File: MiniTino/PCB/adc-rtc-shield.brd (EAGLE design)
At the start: 68.6 x 53.3 mm, 57 parts, among them IC1 TLC2543, IC2 RV_3049_C2

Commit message: Aktualisiert.
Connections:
- net +5V: now also U$1.21
- net A6: now also U$1.A6
- net A7: now also U$1.A7
- net AD0: now also U$1.17
- net AD1: now also U$1.18
- net AD2: now also U$1.19
- net AD3: now also U$1.20
- net AD4/SDA: now also U$1.A4
- net AD5/SCL: now also U$1.A5
- net GND: now also U$1.23
- net IO0: now also U$1.2
- net IO1: now also U$1.1
- net IO2: now also U$1.5
- net IO3: now also U$1.6
- net IO4: now also U$1.7
- net IO5: now also U$1.8
- net IO6: now also U$1.9
- net IO7: now also U$1.10
- net IO8: now also U$1.11
- net IO9: now also U$1.12
- net MISO: now also U$1.15
- net MOSI: now also U$1.14
- net RESET: now also U$1.3
- net SCK: now also U$1.16
- net SS: now also U$1.13
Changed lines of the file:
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@@
 <layer number="49" name="ReferenceLC" color="13" fill="1" visible="no" active="yes"/>
 <layer number="50" name="ReferenceLS" color="12" fill="1" visible="no" active="yes"/>
-<layer number="51" name="tDocu" color="7" fill="1" visible="no" active="yes"/>
+<layer number="51" name="tDocu" color="7" fill="1" visible="yes" active="yes"/>
 <layer number="52" name="bDocu" color="7" fill="1" visible="no" active="yes"/>
 <layer number="91" name="Nets" color="2" fill="1" visible="no" active="no"/>
@@
 <contactref element="JP7" pad="1"/>
 <contactref element="POWER" pad="2"/>
+<contactref element="U$1" pad="21"/>
 <wire x1="40.64" y1="34.29" x2="42.18" y2="36.83" width="0" layer="19" extent="16-16"/>
 <wire x1="34.645" y1="39.91" x2="42.18" y2="36.83" width="0" layer="19" extent="16-16"/>
@@
 <wire x1="38.1" y1="2.54" x2="30.48" y2="2.54" width="0" layer="19" extent="1-1"/>
 <wire x1="44.45" y1="6.35" x2="38.1" y2="2.54" width="0" layer="19" extent="1-1"/>
+<wire x1="-8.89" y1="21.59" x2="7.62" y2="6.35" width="0" layer="19" extent="1-1"/>
 </signal>
 <signal name="GND" class="2">
@@
 <contactref element="JP2" pad="1"/>
 <contactref element="JP3" pad="1"/>
+<contactref element="U$1" pad="23"/>
 <wire x1="44.45" y1="31.75" x2="44.18" y2="36.83" width="0" layer="19" extent="16-16"/>
 <wire x1="37.745" y1="43.91" x2="44.18" y2="36.83" width="0" layer="19" extent="16-16"/>
@@
 <wire x1="44.45" y1="14.875" x2="33.02" y2="11.43" width="0" layer="19" extent="16-16"/>
 <wire x1="4.445" y1="13.97" x2="19.05" y2="13.97" width="0" layer="19" extent="1-1"/>
+<wire x1="-8.89" y1="26.67" x2="4.445" y2="13.97" width="0" layer="19" extent="1-1"/>
 </signal>
 <signal name="AREF" class="4">
@@
 <contactref element="IC2" pad="4"/>
 <contactref element="IC1" pad="18"/>
+<contactref element="U$1" pad="16"/>
 <wire x1="34.645" y1="42.91" x2="28.956" y2="50.8" width="0" layer="19" extent="16-16"/>
 <wire x1="40.64" y1="29.21" x2="34.645" y2="42.91" width="0" layer="19" extent="16-16"/>
+<wire x1="-8.89" y1="8.89" x2="40.64" y2="29.21" width="0" layer="19" extent="1-1"/>
 </signal>
 <signal name="+3V3">
@@
 <contactref element="IC2" pad="5"/>
 <contactref element="IC1" pad="16"/>
+<contactref element="U$1" pad="15"/>
 <wire x1="34.645" y1="43.91" x2="31.496" y2="50.8" width="0" layer="19" extent="16-16"/>
 <wire x1="40.64" y1="24.13" x2="34.645" y2="43.91" width="0" layer="19" extent="16-16"/>
+<wire x1="-8.89" y1="6.35" x2="40.64" y2="24.13" width="0" layer="19" extent="1-1"/>
 </signal>
 <signal name="MOSI">
@@
 <contactref element="IC2" pad="9"/>
 <contactref element="IC1" pad="17"/>
+<contactref element="U$1" pad="14"/>
 <wire x1="37.745" y1="40.91" x2="34.036" y2="50.8" width="0" layer="19" extent="16-16"/>
 <wire x1="40.64" y1="26.67" x2="37.745" y2="40.91" width="0" layer="19" extent="16-16"/>
+<wire x1="-8.89" y1="3.81" x2="40.64" y2="26.67" width="0" layer="19" extent="1-1"/>
 </signal>
 <signal name="SS">
 <contactref element="IOH" pad="3"/>
+<contactref element="U$1" pad="13"/>
+<wire x1="-8.89" y1="1.27" x2="36.576" y2="50.8" width="0" layer="19" extent="1-1"/>
 </signal>
 <signal name="AD0">
 <contactref element="AD" pad="1"/>
+<contactref element="U$1" pad="17"/>
+<wire x1="-8.89" y1="11.43" x2="50.8" y2="2.54" width="0" layer="19" extent="1-1"/>
 </signal>
 <signal name="AD1">
 <contactref element="AD" pad="2"/>
+<contactref element="U$1" pad="18"/>
+<wire x1="-8.89" y1="13.97" x2="53.34" y2="2.54" width="0" layer="19" extent="1-1"/>
 </signal>
 <signal name="AD2">
 <contactref element="AD" pad="3"/>
+<contactref element="U$1" pad="19"/>
+<wire x1="-8.89" y1="16.51" x2="55.88" y2="2.54" width="0" layer="19" extent="1-1"/>
 </signal>
 <signal name="AD3">
 <contactref element="AD" pad="4"/>
+<contactref element="U$1" pad="20"/>
+<wire x1="-8.89" y1="19.05" x2="58.42" y2="2.54" width="0" layer="19" extent="1-1"/>
 </signal>
 <signal name="AD4/SDA">
 <contactref element="IOH" pad="9"/>
 <contactref element="IC2" pad="3"/>
+<contactref element="U$1" pad="A4"/>
 <wire x1="21.336" y1="50.8" x2="34.645" y2="41.91" width="0" layer="19" extent="16-16"/>
+<wire x1="-11.7475" y1="17.93875" x2="21.336" y2="50.8" width="0" layer="19" extent="1-1"/>
 </signal>
 <signal name="AD5/SCL">
 <contactref element="IOH" pad="10"/>
 <contactref element="IC1" pad="15"/>
+<contactref element="U$1" pad="A5"/>
 <wire x1="40.64" y1="21.59" x2="18.796" y2="50.8" width="0" layer="19" extent="1-1"/>
+<wire x1="-11.7475" y1="20.47875" x2="18.796" y2="50.8" width="0" layer="19" extent="1-1"/>
 </signal>
 <signal name="IO2">
 <contactref element="IOL" pad="3"/>
+<contactref element="U$1" pad="5"/>
+<wire x1="-24.13" y1="19.05" x2="58.42" y2="50.8" width="0" layer="19" extent="1-1"/>
 </signal>
 <signal name="IO1">
 <contactref element="IOL" pad="2"/>
+<contactref element="U$1" pad="1"/>
+<wire x1="-24.13" y1="29.21" x2="60.96" y2="50.8" width="0" layer="19" extent="1-1"/>
 </signal>
 <signal name="IO0">
 <contactref element="IOL" pad="1"/>
+<contactref element="U$1" pad="2"/>
+<wire x1="-24.13" y1="26.67" x2="63.5" y2="50.8" width="0" layer="19" extent="1-1"/>
 </signal>
 <signal name="IO3">
 <contactref element="IOL" pad="4"/>
+<contactref element="U$1" pad="6"/>
+<wire x1="-24.13" y1="16.51" x2="55.88" y2="50.8" width="0" layer="19" extent="1-1"/>
 </signal>
 <signal name="IO4">
 <contactref element="IOL" pad="5"/>
+<contactref element="U$1" pad="7"/>
+<wire x1="-24.13" y1="13.97" x2="53.34" y2="50.8" width="0" layer="19" extent="1-1"/>
 </signal>
 <signal name="IO5">
 <contactref element="IOL" pad="6"/>
+<contactref element="U$1" pad="8"/>
+<wire x1="-24.13" y1="11.43" x2="50.8" y2="50.8" width="0" layer="19" extent="1-1"/>
 </signal>
 <signal name="IO6">
 <contactref element="IOL" pad="7"/>
+<contactref element="U$1" pad="9"/>
+<wire x1="-24.13" y1="8.89" x2="48.26" y2="50.8" width="0" layer="19" extent="1-1"/>
 </signal>
 <signal name="IO7">
 <contactref element="IOL" pad="8"/>
+<contactref element="U$1" pad="10"/>
+<wire x1="-24.13" y1="6.35" x2="45.72" y2="50.8" width="0" layer="19" extent="1-1"/>
 </signal>
 <signal name="IO8">
 <contactref element="IOH" pad="1"/>
+<contactref element="U$1" pad="11"/>
+<wire x1="-24.13" y1="3.81" x2="41.656" y2="50.8" width="0" layer="19" extent="1-1"/>
 </signal>
 <signal name="IO9">
 <contactref element="IOH" pad="2"/>
+<contactref element="U$1" pad="12"/>
+<wire x1="-24.13" y1="1.27" x2="39.116" y2="50.8" width="0" layer="19" extent="1-1"/>
 </signal>
 <signal name="X2_TX4-">
@@
 <signal name="RESET">
 <contactref element="POWER" pad="3"/>
+<contactref element="U$1" pad="3"/>
+<wire x1="-24.13" y1="24.13" x2="33.02" y2="2.54" width="0" layer="19" extent="1-1"/>
 </signal>
 <signal name="A6">
 <contactref element="JP8" pad="1"/>
+<contactref element="U$1" pad="A6"/>
+<wire x1="-11.7475" y1="7.46125" x2="-22.86" y2="-5.08" width="0" layer="19" extent="1-1"/>
 </signal>
 <signal name="A7">
 <contactref element="JP8" pad="2"/>
+<contactref element="U$1" pad="A7"/>
+<wire x1="-11.7475" y1="10.00125" x2="-20.32" y2="-5.08" width="0" layer="19" extent="1-1"/>
 </signal>
 </signals>

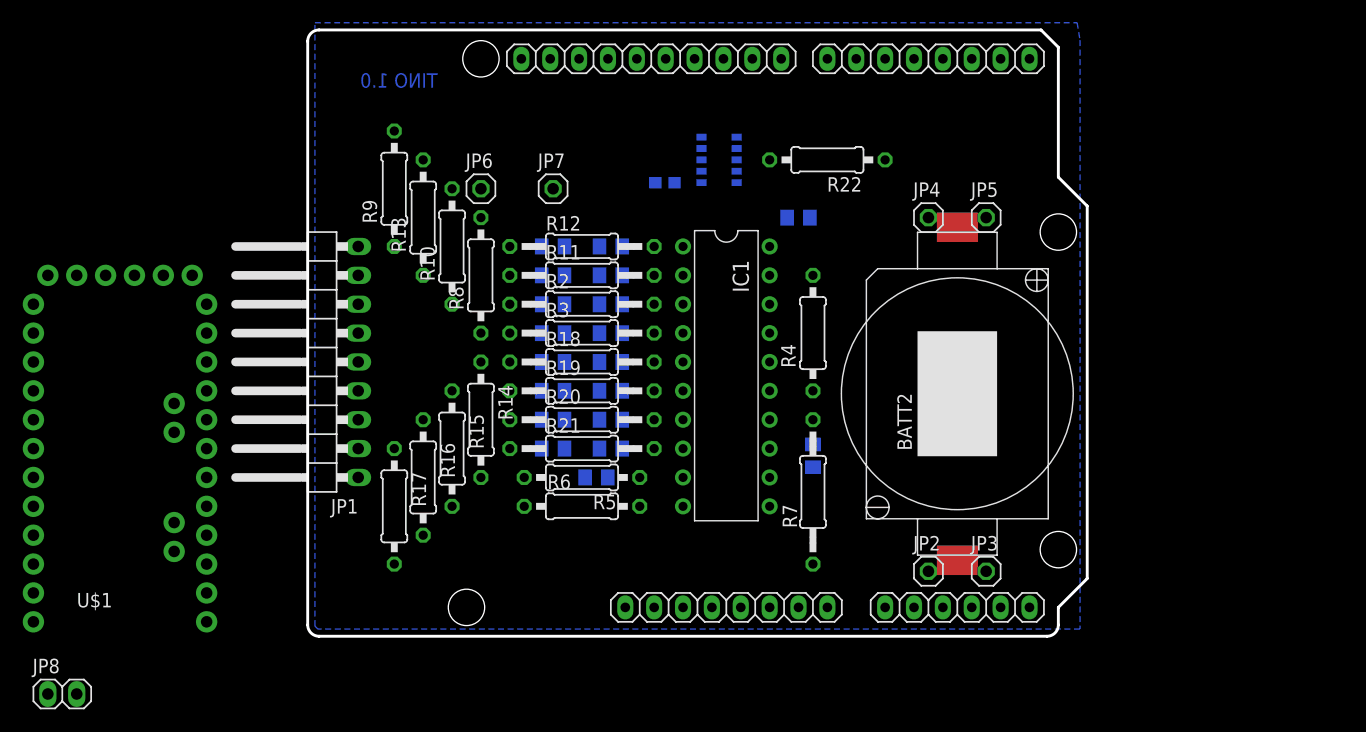
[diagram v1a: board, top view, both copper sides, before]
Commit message: Change resistor packages.
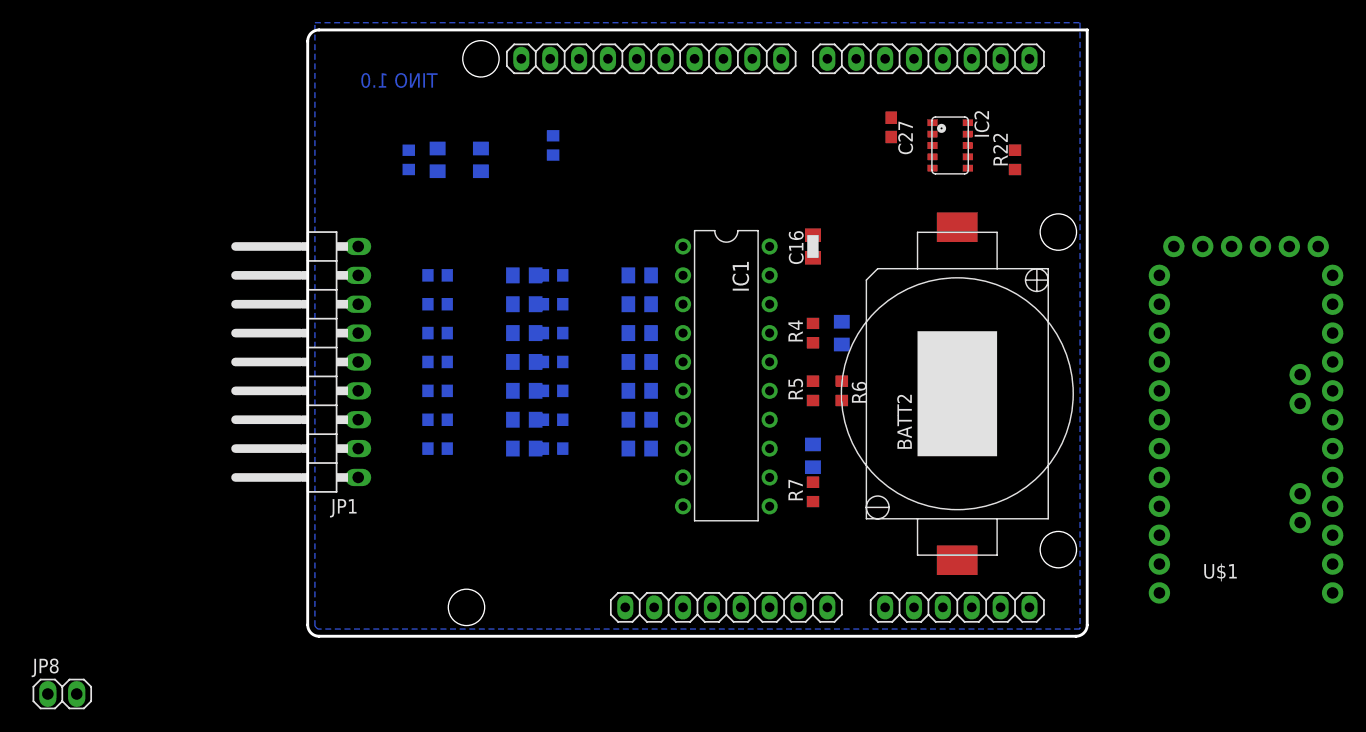
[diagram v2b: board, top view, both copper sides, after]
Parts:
- removed JP2, JP3, JP4, JP5, JP6, JP7: (no value), pinhead:1X01
- R10, R13, R14, R15, R16, R17, R4, R5, R6, R8, R9: device resistor:0207/10 -> resistor:R0603
- R11, R12, R18, R19, R2, R20, R21, R3, R7: device resistor:0207/12 -> resistor:R0603
- R22: device rcl:0207/10 -> rcl:R0603
- moved U$1 99.1 mm to (82.5, 19.1)
- moved C3 25.0 mm to (47.0, 26.7), turned to 270 degrees
- moved R6 25.0 mm to (47.0, 21.6), turned to 270 degrees
- moved R5 21.7 mm to (44.5, 21.6), turned to 90 degrees
- moved C27 20.5 mm to (51.3, 44.8), flipped to the top, turned to 270 degrees
- moved IC2 20.4 mm to (56.5, 43.2), flipped to the top, turned to 270 degrees
- moved R22 16.5 mm to (62.2, 41.9), turned to 90 degrees
- moved C5 13.7 mm to (15.2, 41.9), turned to 90 degrees
- moved C13 12.7 mm to (11.4, 41.9), turned to 90 degrees
- moved R12 9.25 mm to (21.6, 43.2), flipped to the bottom, turned to 270 degrees
- moved R17 6.35 mm to (11.4, 16.5), flipped to the bottom, turned to 180 degrees
- moved R14 6.35 mm to (11.4, 24.1), flipped to the bottom, turned to 180 degrees
- moved R8 6.35 mm to (11.4, 26.7), flipped to the bottom, turned to 180 degrees
- moved R16 5.24 mm to (11.4, 19.1), flipped to the bottom, turned to 180 degrees
- moved R10 5.24 mm to (11.4, 29.2), flipped to the bottom, turned to 180 degrees
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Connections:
- net +5V: no longer JP6.1, JP7.1
- net +BAT: no longer JP4.1, JP5.1
- net GND: no longer JP2.1, JP3.1
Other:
- outline, holes or cut-outs redrawn

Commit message: Start routing.
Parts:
- removed JP8: (no value), pinhead:1X02
- added JP2: (no value), pinhead:1X08/90
- JP1: value 9x1F-H8.5 -> (none); device pinhead:1X09/90 -> pinhead:2X08/90
- moved U$1 40.9 mm to (45.7, 36.8), turned to 270 degrees
- moved R22 40.6 mm to (21.6, 41.3)
- moved BATT2 39.4 mm to (17.8, 20.1)
- moved IC2 38.8 mm to (17.8, 41.9)
- moved C27 37.6 mm to (13.9, 41.6)
- moved C16 24.7 mm to (52.1, 10.8), turned to 0 degrees
- moved IC1 24.0 mm to (53.3, 21.6), turned to 180 degrees
- moved C3 22.2 mm to (36.8, 6.99), flipped to the top, turned to 0 degrees
- moved R6 16.3 mm to (36.8, 8.89), turned to 180 degrees
- moved R4 16.1 mm to (41.9, 10.8), turned to 0 degrees
- moved JP1 14.0 mm to (1.27, 38.1)
- moved R5 13.2 mm to (36.8, 10.8), turned to 0 degrees
- moved C6 9.25 mm to (41.9, 6.99), flipped to the top, turned to 180 degrees
- moved C5 8.98 mm to (24.1, 40.6)
- moved C2 7.18 mm to (24.1, 36.8), turned to 270 degrees
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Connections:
- net +3V3: now also JP2.2
- net +5V: now also JP2.1
- net A6: now also JP2.7; no longer JP8.1
- net A7: now also JP2.8; no longer JP8.2
- net GND: now also JP1.10, JP1.12, JP1.14, JP1.16, JP1.2, JP1.4, JP1.6, JP1.8, JP2.3; no longer JP1.1
- net IO0: now also JP2.5
- net IO1: now also JP2.4
- net RESET: now also JP2.6
- net X1_RX4-: now also JP1.15; no longer JP1.9
- net X2_TX4-: now also JP1.13; no longer JP1.8
- net X3_RX3-: now also JP1.11; no longer JP1.7
- net X4_TX3-: now also JP1.9; no longer JP1.6
- net X5_RX2-: now also JP1.7; no longer JP1.5
- net X6_TX2-: now also JP1.5; no longer JP1.4
- net X8_TX1-: now also JP1.1; no longer JP1.2
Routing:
- net N$18: track 0.00 -> 25.2 mm
- net N$20: track 0.00 -> 21.0 mm
- net N$21: track 0.00 -> 18.2 mm
- net N$22: track 0.00 -> 16.9 mm
- net N$23: track 0.00 -> 16.4 mm
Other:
- outline, holes or cut-outs redrawn
